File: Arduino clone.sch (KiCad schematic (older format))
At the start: 13 parts, among them U1 24LC1025, U2 24LC1025, U3 DS1337S+, U4 ATMEGA328P-AU, Y1 Crystal 32MHz, Y2 Crystal 16MHz

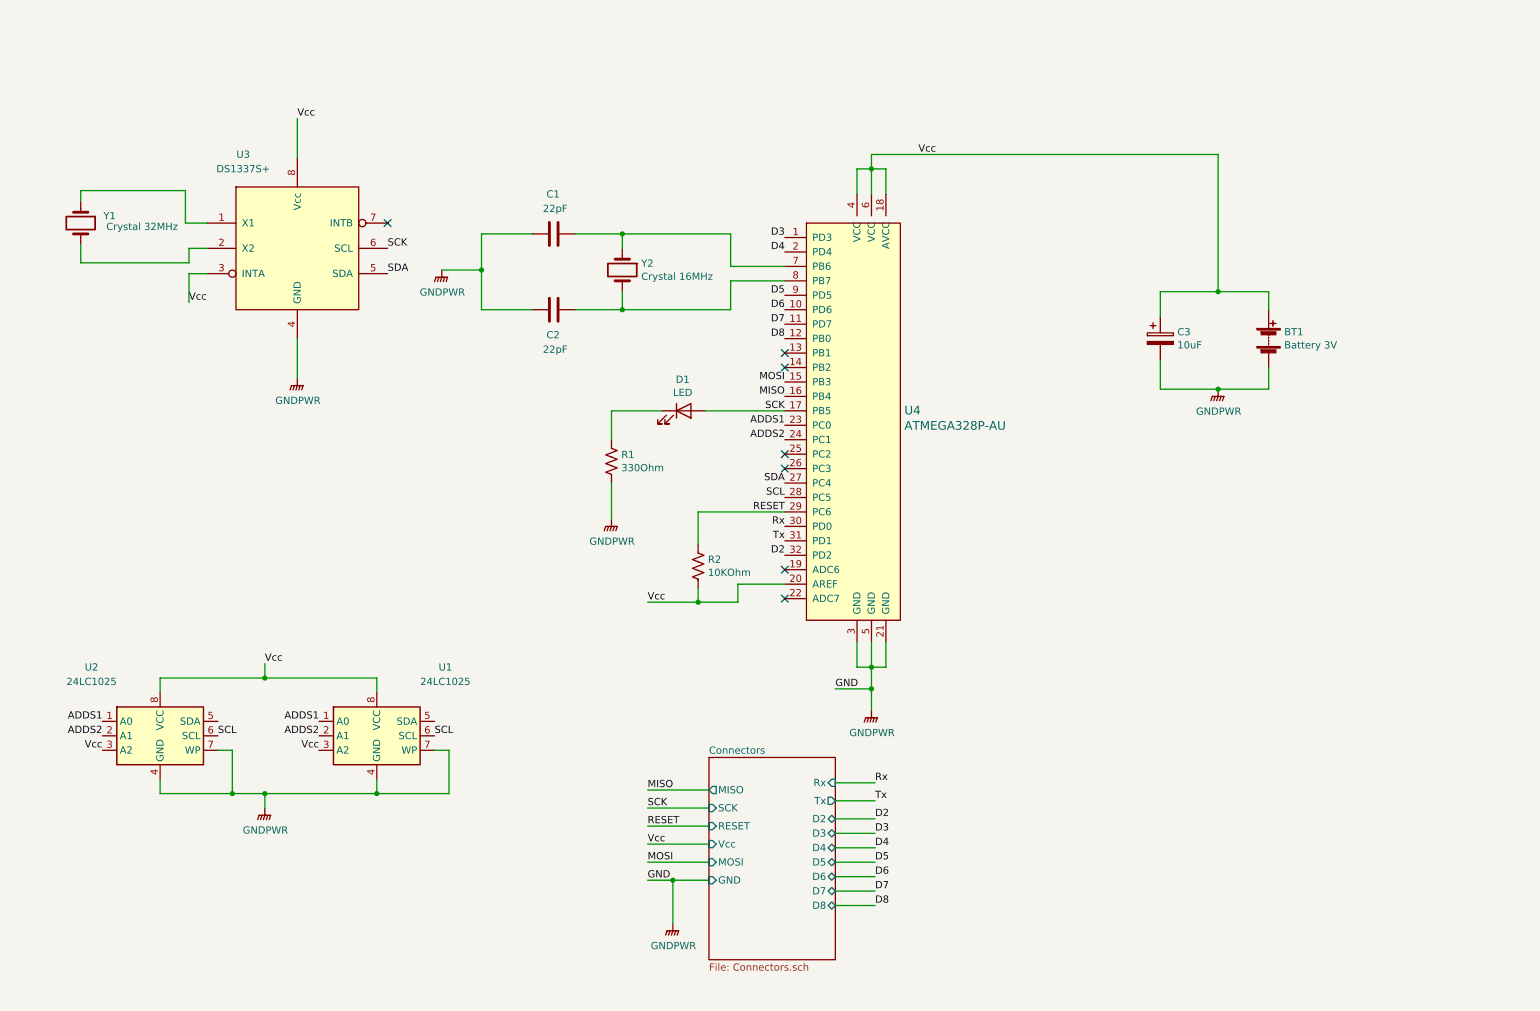
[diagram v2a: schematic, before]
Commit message: Fixed DRC errors
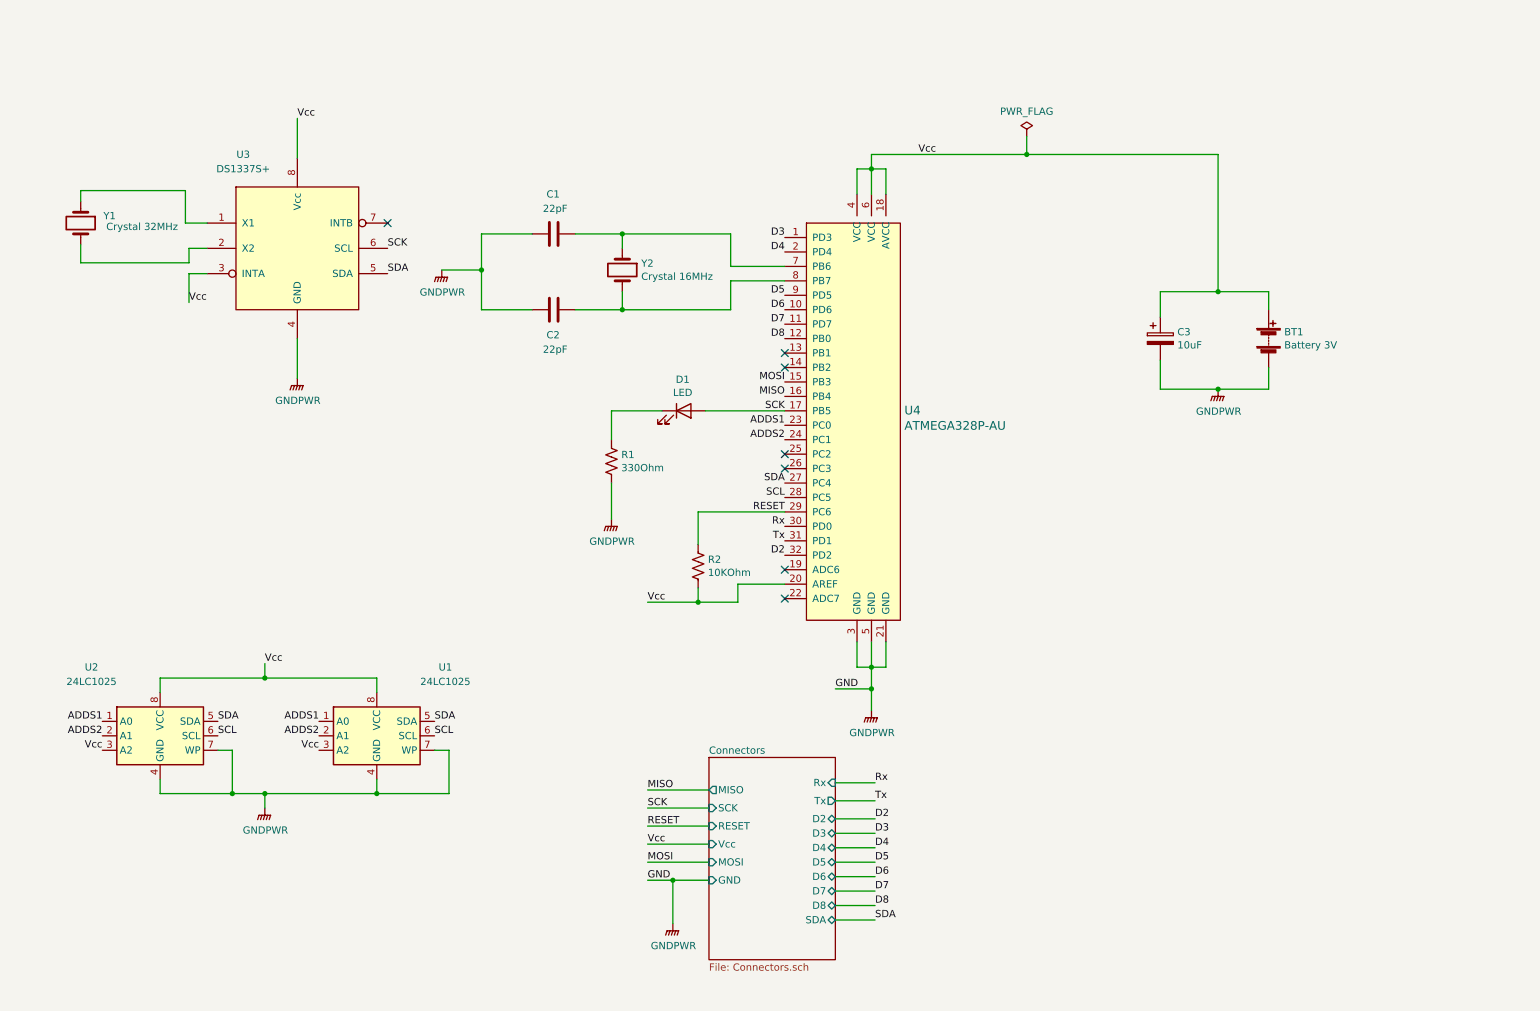
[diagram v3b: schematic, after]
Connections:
- net SDA: now also U1.5 (SDA), U2.5 (SDA)
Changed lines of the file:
@@
 	4950 6825 5125 6825
 $Comp
-L power:GNDPWR #PWR?
+L power:GNDPWR #PWR0101
 U 1 1 602FDDD7
 P 5125 7125
-F 0 "#PWR?" H 5125 6925 50  0001 C CNN
+F 0 "#PWR0101" H 5125 6925 50  0001 C CNN
 F 1 "GNDPWR" H 5129 6971 50  0000 C CNN
 F 2 "" H 5125 7075 50  0001 C CNN
@@
 F15 "D7" B R 6250 6900 50
 F16 "D8" B R 6250 7000 50
+F17 "SDA" B R 6250 7100 50
 $EndSheet
 Wire Wire Line
@@
 	1775 2450 1900 2450
 $Comp
-L power:GNDPWR #PWR?
+L power:GNDPWR #PWR0102
 U 1 1 6032B290
 P 2525 3350
-F 0 "#PWR?" H 2525 3150 50  0001 C CNN
+F 0 "#PWR0102" H 2525 3150 50  0001 C CNN
 F 1 "GNDPWR" H 2529 3196 50  0000 C CNN
 F 2 "" H 2525 3300 50  0001 C CNN
@@
 Connection ~ 2300 5425
 $Comp
-L power:GNDPWR #PWR?
+L power:GNDPWR #PWR0103
 U 1 1 6033BDFB
 P 2300 6325
-F 0 "#PWR?" H 2300 6125 50  0001 C CNN
+F 0 "#PWR0103" H 2300 6125 50  0001 C CNN
 F 1 "GNDPWR" H 2304 6171 50  0000 C CNN
 F 2 "" H 2300 6275 50  0001 C CNN
@@
 ADDS2
 $Comp
-L power:GNDPWR #PWR?
+L power:GNDPWR #PWR0104
 U 1 1 6034A20E
 P 8900 3425
-F 0 "#PWR?" H 8900 3225 50  0001 C CNN
+F 0 "#PWR0104" H 8900 3225 50  0001 C CNN
 F 1 "GNDPWR" H 8904 3271 50  0000 C CNN
 F 2 "" H 8900 3375 50  0001 C CNN
@@
 	8900 2750 8900 1800
 Wire Wire Line
-	8900 1800 6500 1800
+	8900 1800 7575 1800
 Connection ~ 8900 2750
 Wire Wire Line
@@
 	4775 2750 4775 2875
 $Comp
-L power:GNDPWR #PWR?
+L power:GNDPWR #PWR0105
 U 1 1 60361C9D
 P 3525 2600
-F 0 "#PWR?" H 3525 2400 50  0001 C CNN
+F 0 "#PWR0105" H 3525 2400 50  0001 C CNN
 F 1 "GNDPWR" H 3529 2446 50  0000 C CNN
 F 2 "" H 3525 2550 50  0001 C CNN
@@
 	5350 3575 5900 3575
 $Comp
-L power:GNDPWR #PWR?
+L power:GNDPWR #PWR0106
 U 1 1 60374741
 P 4700 4325
-F 0 "#PWR?" H 4700 4125 50  0001 C CNN
+F 0 "#PWR0106" H 4700 4125 50  0001 C CNN
 F 1 "GNDPWR" H 4704 4171 50  0000 C CNN
 F 2 "" H 4700 4275 50  0001 C CNN
@@
 Connection ~ 5300 4900
 $Comp
-L power:GNDPWR #PWR?
+L power:GNDPWR #PWR0107
 U 1 1 60381923
 P 6500 5650
-F 0 "#PWR?" H 6500 5450 50  0001 C CNN
+F 0 "#PWR0107" H 6500 5450 50  0001 C CNN
 F 1 "GNDPWR" H 6504 5496 50  0000 C CNN
 F 2 "" H 6500 5600 50  0001 C CNN
@@
 NoConn ~ 5900 4675
 NoConn ~ 5900 4875
+Text Label 1975 5725 0    50   ~ 0
+SDA
+Text Label 3475 5725 0    50   ~ 0
+SDA
+Text Label 6525 7100 0    50   ~ 0
+SDA
+Wire Wire Line
+	6250 7100 6525 7100
+$Comp
+L power:PWR_FLAG #FLG0101
+U 1 1 603A3749
+P 7575 1675
+F 0 "#FLG0101" H 7575 1750 50  0001 C CNN
+F 1 "PWR_FLAG" H 7575 1848 50  0000 C CNN
+F 2 "" H 7575 1675 50  0001 C CNN
+F 3 "~" H 7575 1675 50  0001 C CNN
+	1    7575 1675
+	1    0    0    -1
+$EndComp
+Wire Wire Line
+	7575 1675 7575 1800
+Connection ~ 7575 1800
+Wire Wire Line
+	7575 1800 6500 1800
 $EndSCHEMATC

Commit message: Added functional block descriptions
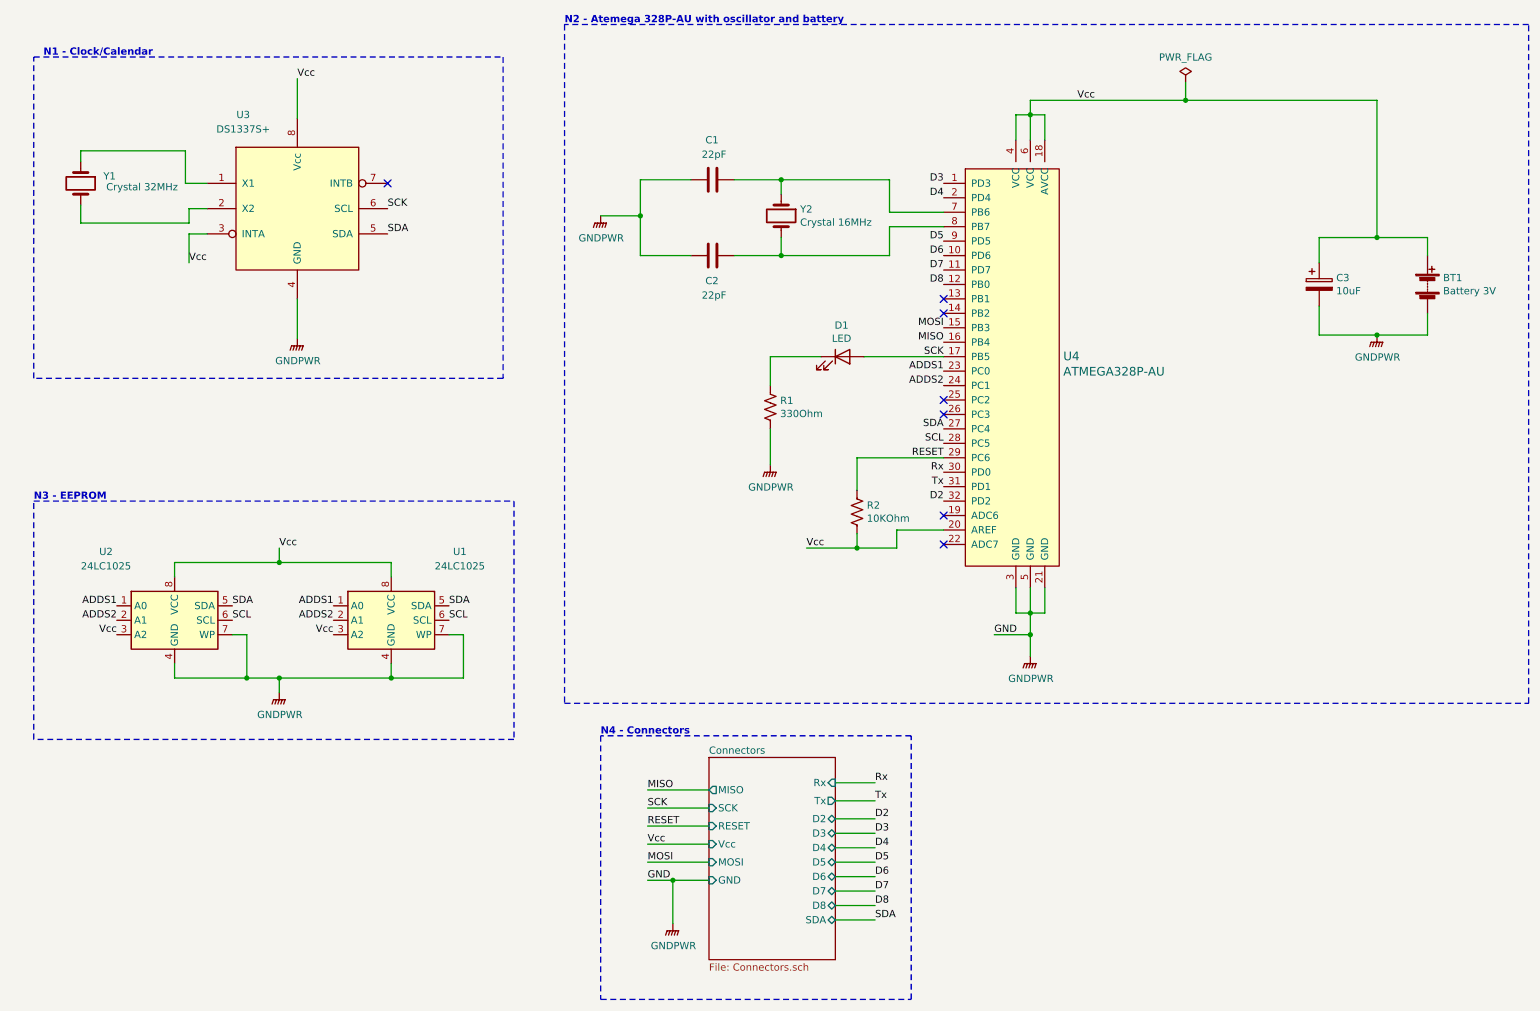
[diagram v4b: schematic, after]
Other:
- note added: "N1 - Clock/Calendar"
- note added: "N2 - Atemega 328P-AU with oscillator and battery"
- note added: "N3 - EEPROM"
- note added: "N4 - Connectors"
- moved on the sheet: BT1, C1, C2, C3, D1, R1, R2, U1, U2, U3, U4, Y1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
